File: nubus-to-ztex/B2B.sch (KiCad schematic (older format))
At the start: 13 parts, among them J1 87832-1420 (2x7 M 2mm), J3 Conn_01x06_Male

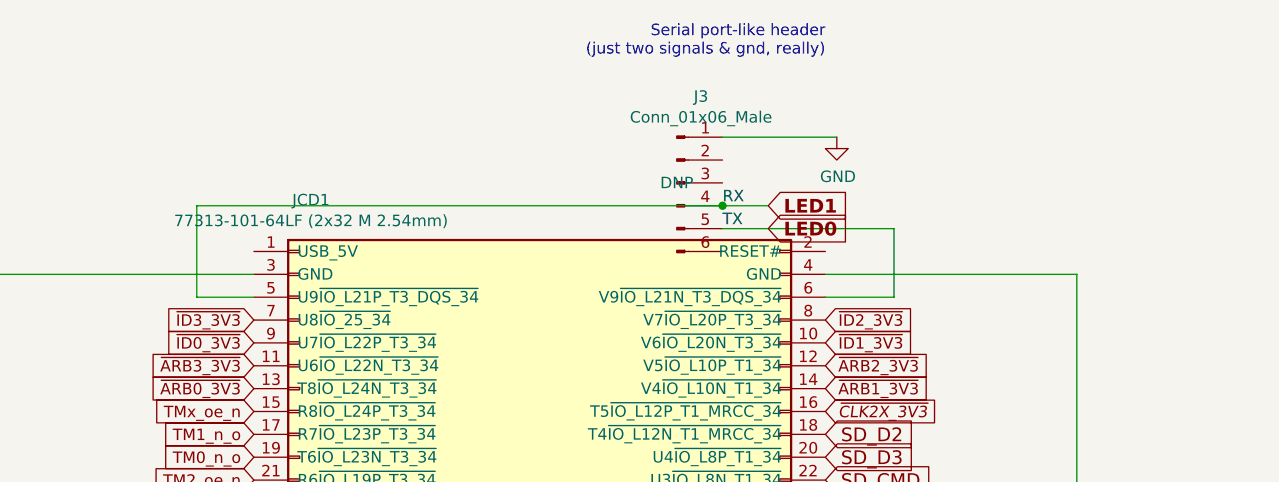
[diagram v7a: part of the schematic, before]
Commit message: BoM, power plane, serial back to THT, ...
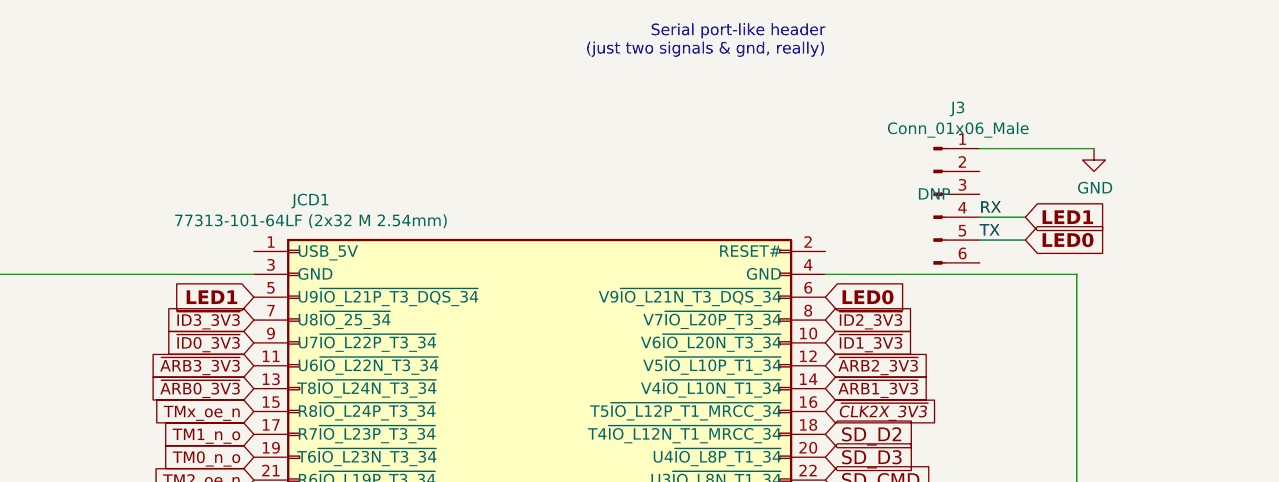
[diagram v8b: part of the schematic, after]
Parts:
- C1, C2: URL https://lcsc.com/product-detail/Multilayer-Ceramic-Capacito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 -> https://www.lcsc.com/product-detail/Multilayer-Ceramic-Capa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
- C3: MPN GRM21BR61A476ME15K -> C2012X5R1A476MTJ00E; URL https://www.lcsc.com/product-detail/Multilayer-Ceramic-Capacitors-MLCC-SMD-SMT_Murata-Electronics-GRM21BR61A476ME15K_C2292827.html -> https://www.lcsc.com/product-detail/Multilayer-Ceramic-Capacitors-MLCC-SMD-SMT_TDK-C2012X5R1A476MTJ00E_C76636.html
- J3: footprint For_SeeedStudio:SAMTEC_TSM-106-01-L-SH -> For_SeeedStudio:PinHeader_1x06_P2.54mm_Horizontal_For_SeeedStudio; MPN TSM-106-01-T-SH -> (none); MPN comments 'T' is tin 'L' is gold ; with extra -A (and footprint chang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 -> (none); URL https://www.mouser.fr/ProductDetail/Samtec/TSM-106-01-T-SH?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 -> (none)
- JAB1, JCD1: MPN 77313-101-64LF -> 10-89-7642; MPN (Amphenol) (none) -> 77313-101-64LF; URL https://eu.mouser.com/ProductDetail/Amphenol-FCI/77313-101-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 -> https://www.mouser.fr/ProductDetail/Molex/10-89-7642?qs=oWQ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; URL (Amphenol) (none) -> https://eu.mouser.com/ProductDetail/Amphenol-FCI/77313-101-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
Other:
- moved on the sheet: J3
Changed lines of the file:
@@
 F 6 "X6521WV-2x32H-C30D60" H 1800 2650 50  0001 C CNN "MPN (XKB)"
 F 7 "https://www.lcsc.com/product-detail/Pin-Headers_XKB-Connectivity-X6521WV-2x32H-C30D60_C2883966.html" H 1800 2650 50  0001 C CNN "URL (XKB)"
-F 8 "77313-101-64LF" H 1800 2650 50  0001 C CNN "MPN"
-F 9 "https://eu.mouser.com/ProductDetail/Amphenol-FCI/77313-101-64LF?qs=xJiur%252Bgubk1MSan%2F7C0v%252BA%3D%3D" H 1800 2650 50  0001 C CNN "URL"
+F 8 "77313-101-64LF" H 1800 2650 50  0001 C CNN "MPN (Amphenol)"
+F 9 "https://eu.mouser.com/ProductDetail/Amphenol-FCI/77313-101-64LF?qs=xJiur%252Bgubk1MSan%2F7C0v%252BA%3D%3D" H 1800 2650 50  0001 C CNN "URL (Amphenol)"
+F 10 "10-89-7642" H 1800 2650 50  0001 C CNN "MPN"
+F 11 "https://www.mouser.fr/ProductDetail/Molex/10-89-7642?qs=oWQp3ZoCHH1BnT8RSmq80A%3D%3D" H 1800 2650 50  0001 C CNN "URL"
 	1    1800 2650
 	1    0    0    -1
@@
 	7150 2850 6700 2850
 $Comp
-L Connector:Conn_01x06_Male J3
-U 1 1 5F69129B
-P 9250 850
-F 0 "J3" H 9356 1228 50  0000 C CNN
-F 1 "Conn_01x06_Male" H 9356 1137 50  0000 C CNN
-F 2 "For_SeeedStudio:SAMTEC_TSM-106-01-L-SH" H 9250 850 50  0001 C CNN
-F 3 "https://www.mouser.com/datasheet/2/527/tsm-2854655.pdf" H 9250 850 50  0001 C CNN
-F 4 "TSM-106-01-T-SH" H 9250 850 50  0001 C CNN "MPN"
-F 5 "https://www.mouser.fr/ProductDetail/Samtec/TSM-106-01-T-SH?qs=0lQeLiL1qybjt4R2%252BGOpsA%3D%3D" H 9250 850 50  0001 C CNN "URL"
-F 6 "'T' is tin 'L' is gold ; with extra -A (and footprint change) to get alignment pin ; -01 is post length (-02 would be fine)" H 9250 850 50  0001 C CNN "MPN comments"
-F 7 "DNP" H 9250 850 50  0000 C CNN "DNP"
-	1    9250 850
-	1    0    0    -1
-$EndComp
-$Comp
 L power:GND #PWR018
 U 1 1 5F6913A1
-P 9950 650
-F 0 "#PWR018" H 9950 400 50  0001 C CNN
-F 1 "GND" H 9955 477 50  0000 C CNN
-F 2 "" H 9950 650 50  0001 C CNN
-F 3 "" H 9950 650 50  0001 C CNN
-	1    9950 650
-	1    0    0    -1
-$EndComp
-Wire Wire Line
-	9450 650  9950 650
-Wire Wire Line
-	9450 950  7150 950
-Wire Wire Line
-	7150 950  7150 1350
-Text Label 9450 1050 0    50   ~ 0
+P 11075 700
+F 0 "#PWR018" H 11075 450 50  0001 C CNN
+F 1 "GND" H 11080 527 50  0000 C CNN
+F 2 "" H 11075 700 50  0001 C CNN
+F 3 "" H 11075 700 50  0001 C CNN
+	1    11075 700
+	1    0    0    -1
+$EndComp
+Wire Wire Line
+	10575 700  11075 700
+Text Label 10575 1100 0    50   ~ 0
 TX
-Text Label 9450 950  0    50   ~ 0
+Text Label 10575 1000 0    50   ~ 0
 RX
 $Comp
@@
 F 6 "X6521WV-2x32H-C30D60" H 1800 2650 50  0001 C CNN "MPN (XKB)"
 F 7 "https://www.lcsc.com/product-detail/Pin-Headers_XKB-Connectivity-X6521WV-2x32H-C30D60_C2883966.html" H 1800 2650 50  0001 C CNN "URL (XKB)"
-F 8 "77313-101-64LF" H 1800 2650 50  0001 C CNN "MPN"
-F 9 "https://eu.mouser.com/ProductDetail/Amphenol-FCI/77313-101-64LF?qs=xJiur%252Bgubk1MSan%2F7C0v%252BA%3D%3D" H 1800 2650 50  0001 C CNN "URL"
+F 8 "77313-101-64LF" H 1800 2650 50  0001 C CNN "MPN (Amphenol)"
+F 9 "https://eu.mouser.com/ProductDetail/Amphenol-FCI/77313-101-64LF?qs=xJiur%252Bgubk1MSan%2F7C0v%252BA%3D%3D" H 1800 2650 50  0001 C CNN "URL (Amphenol)"
+F 10 "10-89-7642" H 7600 2650 50  0001 C CNN "MPN"
+F 11 "https://www.mouser.fr/ProductDetail/Molex/10-89-7642?qs=oWQp3ZoCHH1BnT8RSmq80A%3D%3D" H 7600 2650 50  0001 C CNN "URL"
 	1    7600 2650
 	1    0    0    -1
@@
 	7150 2650 7400 2650
 Wire Wire Line
-	7150 1350 7400 1350
-Wire Wire Line
 	1450 2550 1600 2550
 Wire Wire Line
@@
 $EndComp
 Connection ~ 500  4450
-Wire Wire Line
-	10200 1050 10200 1350
-Wire Wire Line
-	10200 1350 9900 1350
 Text GLabel 4100 2050 2    50   Input Italic 0
 ~CLK_3V3
@@
 Text GLabel 1850 6400 2    60   Input ~ 12
 LED1
-Text GLabel 9650 1050 2    60   Input ~ 12
+Text GLabel 9900 1350 2    60   Input ~ 12
 LED0
-Text GLabel 9650 950  2    60   Input ~ 12
+Text GLabel 10775 1000 2    60   Input ~ 12
 LED1
 Text GLabel 1600 4050 0    50   Input ~ 0
@@
 F 9 "?" H 3000 6050 50  0001 C CNN "Koncar"
 F 10 "TB" H 3000 6050 50  0001 C CNN "Side"
-F 11 "https://lcsc.com/product-detail/Multilayer-Ceramic-Capacitors-MLCC-SMD-SMT_YAGEO-CC0603KRX7R8BB104_C92490.html" H 3000 6050 50  0001 C CNN "URL"
+F 11 "https://www.lcsc.com/product-detail/Multilayer-Ceramic-Capacitors-MLCC-SMD-SMT_YAGEO-CC0603KRX7R8BB104_C92490.html" H 3000 6050 50  0001 C CNN "URL"
 	1    3000 6050
 	1    0    0    -1
@@
 F 9 "?" H 3400 6050 50  0001 C CNN "Koncar"
 F 10 "TB" H 3400 6050 50  0001 C CNN "Side"
-F 11 "https://lcsc.com/product-detail/Multilayer-Ceramic-Capacitors-MLCC-SMD-SMT_YAGEO-CC0603KRX7R8BB104_C92490.html" H 3400 6050 50  0001 C CNN "URL"
+F 11 "https://www.lcsc.com/product-detail/Multilayer-Ceramic-Capacitors-MLCC-SMD-SMT_YAGEO-CC0603KRX7R8BB104_C92490.html" H 3400 6050 50  0001 C CNN "URL"
 	1    3400 6050
 	1    0    0    -1
@@
 F 4 "C2012X5R1A476MTJ00E" H 4000 6050 50  0001 C CNN "MPN-ALT"
 F 5 "https://lcsc.com/product-detail/Multilayer-Ceramic-Capacitors-MLCC-SMD-SMT_TDK-C2012X5R1A476MTJ00E_C76636.html" H 4000 6050 50  0001 C CNN "URL-ALT"
-F 6 "GRM21BR61A476ME15K" H 4000 6050 50  0001 C CNN "MPN"
-F 7 "https://www.lcsc.com/product-detail/Multilayer-Ceramic-Capacitors-MLCC-SMD-SMT_Murata-Electronics-GRM21BR61A476ME15K_C2292827.html" H 4000 6050 50  0001 C CNN "URL"
+F 6 "C2012X5R1A476MTJ00E" H 4000 6050 50  0001 C CNN "MPN"
+F 7 "https://www.lcsc.com/product-detail/Multilayer-Ceramic-Capacitors-MLCC-SMD-SMT_TDK-C2012X5R1A476MTJ00E_C76636.html" H 4000 6050 50  0001 C CNN "URL"
 	1    4000 6050
 	1    0    0    -1
@@
 $EndComp
 Wire Wire Line
-	9450 950  9650 950
-Connection ~ 9450 950
-Wire Wire Line
-	9450 1050 10200 1050
+	10575 1000 10775 1000
+$Comp
+L Connector:Conn_01x06_Male J3
+U 1 1 5F69129B
+P 10375 900
+F 0 "J3" H 10481 1278 50  0000 C CNN
+F 1 "Conn_01x06_Male" H 10481 1187 50  0000 C CNN
+F 2 "For_SeeedStudio:PinHeader_1x06_P2.54mm_Horizontal_For_SeeedStudio" H 10375 900 50  0001 C CNN
+F 3 "" H 10375 900 50  0001 C CNN
+F 4 "" H 10375 900 50  0001 C CNN "MPN"
+F 5 "" H 10375 900 50  0001 C CNN "URL"
+F 6 "DNP" H 10375 900 50  0000 C CNN "DNP"
+	1    10375 900
+	1    0    0    -1
+$EndComp
+Text GLabel 7400 1350 0    60   Input ~ 12
+LED1
+Text GLabel 10775 1100 2    60   Input ~ 12
+LED0
+Wire Wire Line
+	10575 1100 10775 1100
 $EndSCHEMATC
